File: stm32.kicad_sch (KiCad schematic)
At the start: 31 parts, among them J1 Screw_Terminal_01x04, J5 Screw_Terminal_01x08, U1 STM32H743VITx, U8 REF3030, Y1 20Mhz

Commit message: avance de pcb, se considera borneras externas para conexión de alimentación
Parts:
- removed C12: 100nF 50V, symbol Device:C
- removed C13: 1uF 50V, symbol Device:C
- removed J5: Screw_Terminal_01x08, symbol Connector:Screw_Terminal_01x08
- removed J9: ~, symbol Connector:Screw_Terminal_01x02
- added C95: 2u2F/50V, Capacitor_SMD:C_0805_2012Metric, symbol 1-Capacitor:C_0805
- added JP1: Jumper_2_Bridged, Jumper:SolderJumper-2_P1.3mm_Open_Pad1.0x1.5mm, symbol Jumper:Jumper_2_Bridged
- C74: renamed from C41; value 100nF 50V -> 100nF/50V; footprint 1-Capacitor:C_0603_1608Metric -> Capacitor_SMD:C_0603_1608Metric
- C75: renamed from C20; value ~ -> 30pF/50V; footprint (none) -> Capacitor_SMD:C_0603_1608Metric
- C76: renamed from C11; value 100nF 50V -> 100nF/50V; footprint (none) -> Capacitor_SMD:C_0603_1608Metric
- C77: renamed from C42; value 100nF 50V -> 100nF/50V; footprint 1-Capacitor:C_0603_1608Metric -> Capacitor_SMD:C_0603_1608Metric
- C78: renamed from C21; value ~ -> 30pF/50V; footprint (none) -> Capacitor_SMD:C_0603_1608Metric
- C79: renamed from C16; value 2u2F 25V -> 2u2F/50V; footprint (none) -> Capacitor_SMD:C_0805_2012Metric
- C80: renamed from C17; value 2u2F 25V -> 2u2F/50V; footprint (none) -> Capacitor_SMD:C_0805_2012Metric
- C81: renamed from C18; value 2u2F 25V -> 2u2F/50V; footprint (none) -> Capacitor_SMD:C_0805_2012Metric
- C82: renamed from C19; value 2u2F 25V -> 2u2F/50V; footprint (none) -> Capacitor_SMD:C_0805_2012Metric
- C83: renamed from C1; value 100nF 50V -> 100nF/50V; footprint (none) -> Capacitor_SMD:C_0603_1608Metric
- C84: renamed from C2; value 10nF 50V -> 10nF/50V; footprint (none) -> Capacitor_SMD:C_0603_1608Metric
- C85: renamed from C3; value 100nF 50V -> 100nF/50V; footprint (none) -> Capacitor_SMD:C_0603_1608Metric
- C86: renamed from C14; value 10nF 50V -> 10nF/50V; footprint (none) -> Capacitor_SMD:C_0603_1608Metric
- C87: renamed from C15; value 100nF 50V -> 100nF/50V; footprint (none) -> Capacitor_SMD:C_0603_1608Metric
- C88: renamed from C4; value 10nF 50V -> 10nF/50V; footprint (none) -> Capacitor_SMD:C_0603_1608Metric
- C89: renamed from C5; value 100nF 50V -> 100nF/50V; footprint (none) -> Capacitor_SMD:C_0603_1608Metric
- C90: renamed from C6; value 10nF 50V -> 10nF/50V; footprint (none) -> Capacitor_SMD:C_0603_1608Metric
- C91: renamed from C7; value 100nF 50V -> 100nF/50V; footprint (none) -> Capacitor_SMD:C_0603_1608Metric
- C92: renamed from C8; value 10nF 50V -> 10nF/50V; footprint (none) -> Capacitor_SMD:C_0603_1608Metric
- C93: renamed from C9; value 100nF 50V -> 100nF/50V; footprint (none) -> Capacitor_SMD:C_0603_1608Metric
- C94: renamed from C10; value 10nF 50V -> 10nF/50V; footprint (none) -> Capacitor_SMD:C_0603_1608Metric
- FB2: renamed from FB1; value 100R -> 600R
- J13: renamed from J1; footprint (none) -> Connector_PinHeader_2.54mm:PinHeader_1x04_P2.54mm_Vertical
- R116: renamed from R1; footprint (none) -> Resistor_SMD:R_0603_1608Metric
- Y4: renamed from Y1; value 20Mhz -> 8Mhz; footprint (none) -> Crystal:Crystal_SMD_5032-2Pin_5.0x3.2mm
- renumbered U8 to U22, U1 to U23
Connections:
- net ETH_nRST: now also JP1.1 (A); no longer U23.63 (PC6)
- net GND: now also C95.2
- net VDD_3V3: now also C95.1
- net nRST: now also JP1.2 (B)
- net Relay_8: now reaches U23.67 (PA8)
- net Relay_9: now reaches U23.68 (PA9)
- net Relay_10: now reaches U23.69 (PA10)
- net Relay_12: now reaches U23.71 (PA12)
- net CS1: now reaches U23.84 (PD3)
- net RDY2: now reaches U23.85 (PD4)
- net CS2: now reaches U23.86 (PD5)
- net DIG_1: now reaches U23.90 (PB4)
- net DIG_4: now reaches U23.93 (PB7)
- net DIG_5: now reaches U23.95 (PB8)
- net DIG_6: now reaches U23.96 (PB9)
- net DIG_7: now reaches U23.97 (PE0)
- net DIG_8: now reaches U23.98 (PE1)
- net ADC1_10: no longer names the net of U23.15 (PC0)
- net ADC1_15: no longer names the net of U23.25 (PA3)
- net ADC1_16: no longer names the net of U23.22 (PA0)
- net ADC1_18: no longer names the net of U23.28 (PA4)
- net ADC1_19: no longer names the net of U23.29 (PA5)
- net ADC1_3: no longer names the net of U23.30 (PA6)
- net ADC1_5: no longer names the net of U23.35 (PB1)
- net ADC1_9: no longer names the net of U23.34 (PB0)
- net DO1: no longer names the net of U23.55 (PD8)
- net DO2: no longer names the net of U23.56 (PD9)
- net DO3: no longer names the net of U23.57 (PD10)
- net DO4: no longer names the net of U23.58 (PD11)
- net DO5: no longer names the net of U23.59 (PD12)
- net DO6 renamed Relay_1
- net DO7 renamed Relay_2
- net DO8 renamed Relay_3
- net PLL_CLK: no longer names the net of U23.3 (PE4)
- net PLL_DIN renamed DIG_9
- net PLL_ENB: no longer names the net of U23.2 (PE3)
- net PLL_LD: no longer names the net of U23.4 (PE5)
- net PLL_RST: no longer names the net of U23.5 (PE6)
- net PWM1_1: no longer names the net of U23.39 (PE9)
- net PWM1_2: no longer names the net of U23.41 (PE11)
- net SDMMC1_CK renamed ADS_MOSI
- net SDMMC1_CMD renamed RDY1
- net SDMMC1_D0 renamed Relay_6
- net SDMMC1_D1 renamed Relay_7
- net SDMMC1_D2 renamed ADS_SCLK
- net SDMMC1_D3 renamed ADS_MISO
- net SDMMC1_SW renamed Relay_5
- net SPI2_MISO: no longer names the net of U23.17 (PC2_C)
- net SPI2_MOSI: no longer names the net of U23.18 (PC3_C)
- net SPI2_NSS renamed Relay_11
- net SPI2_SCK: no longer names the net of U23.46 (PB10)
- net UART5_RX renamed DIG_2
- net UART5_TX renamed DIG_3
- new net Relay_4: U23.63 (PC6)
- no-connect marks 31 -> 40
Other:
- note added: "C1002"
- note added: "C115962"
- note added: "C377773"
- note added: "Don't use it if it is not necessary"
- note removed: "ADC"
- note removed: "DEBUG"
- note removed: "DIGITAL OUTPUT"
- note removed: "ETHERNET"
- note removed: "HMI"
- note removed: "PWM"
- note removed: "SD CARD"
- note removed: "WIFI"
- moved on the sheet: C74, C75, C76, C77, C78, C79, C80, C81, C82, C83, C84, C85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

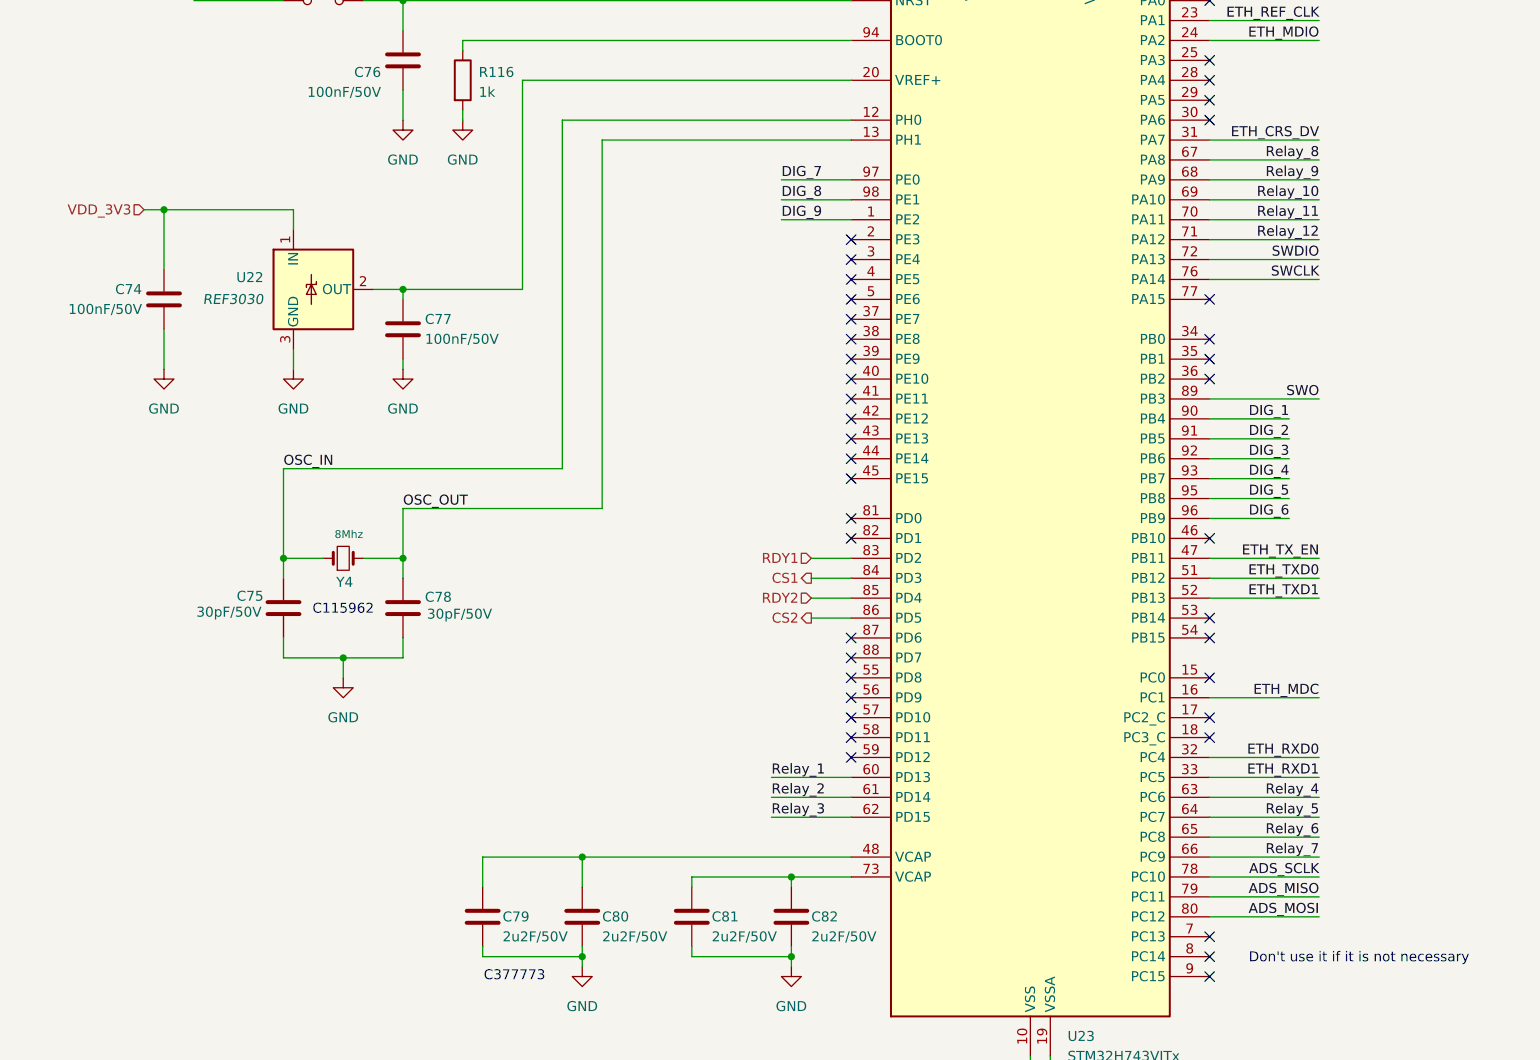
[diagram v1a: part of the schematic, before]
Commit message: Se empieza a evaluar la conexión del ethernet con la carcasa, parte analog, dig y micro en posición, tambien se busca solución para la salida de led de las entradas digitales
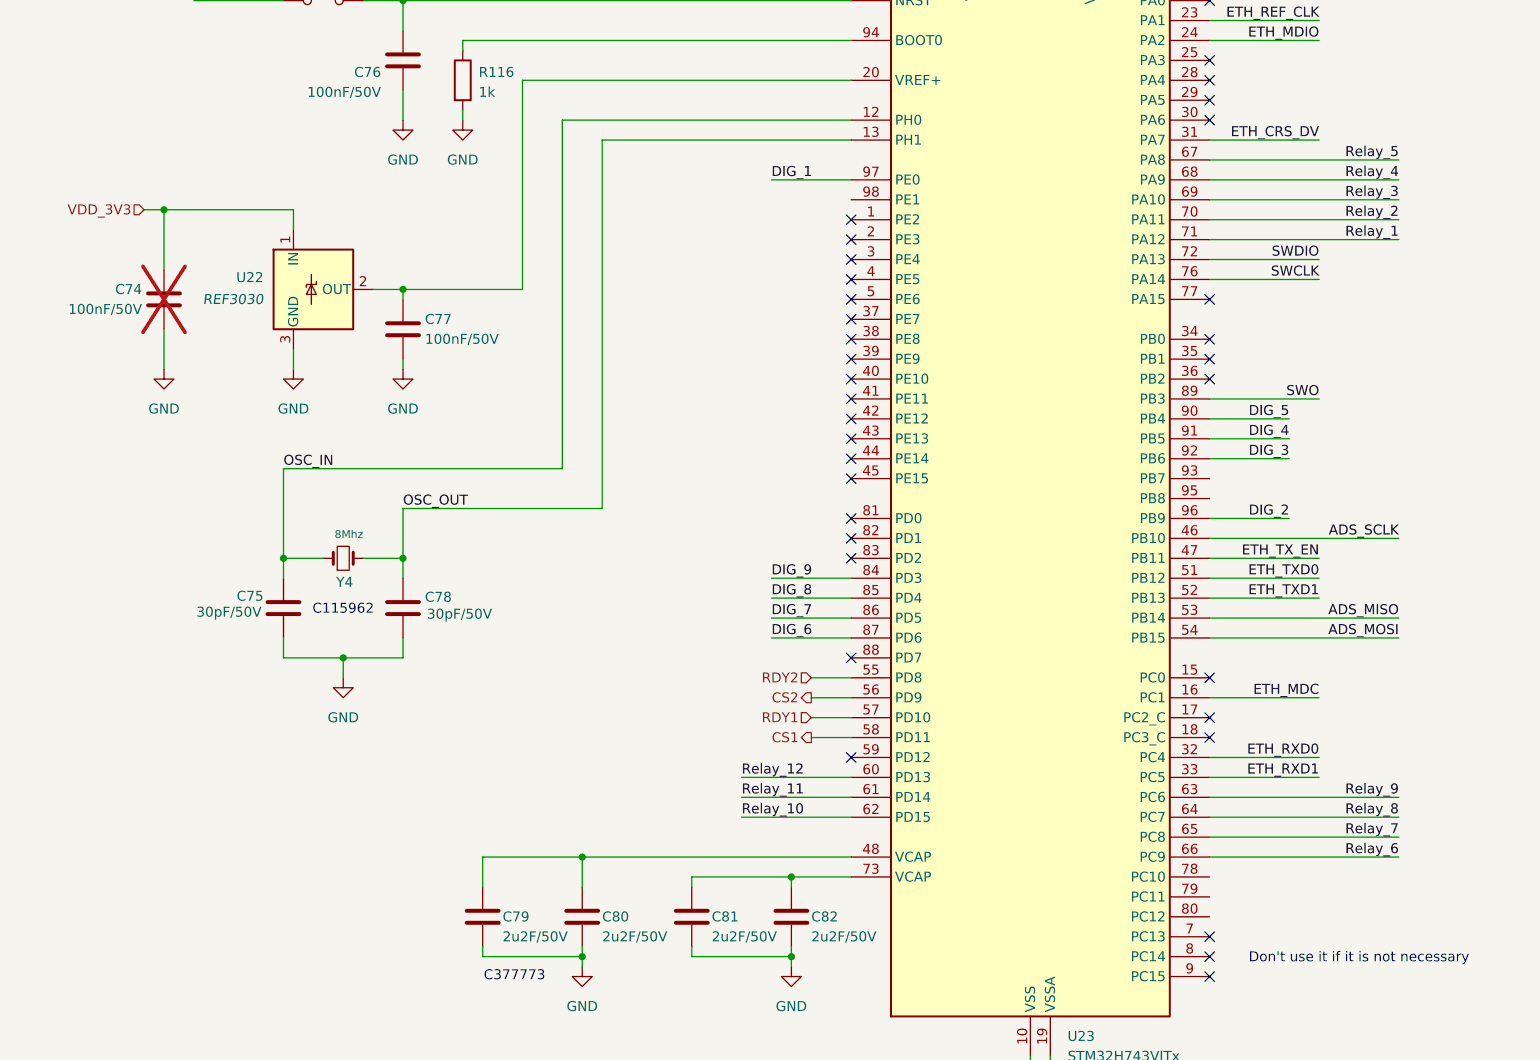
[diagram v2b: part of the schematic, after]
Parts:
- C74: now not fitted
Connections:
- net ADS_MISO: now also U23.53 (PB14); no longer U23.79 (PC11)
- net ADS_MOSI: now also U23.54 (PB15); no longer U23.80 (PC12)
- net ADS_SCLK: now also U23.46 (PB10); no longer U23.78 (PC10)
- net CS1: now also U23.58 (PD11); no longer U23.84 (PD3)
- net CS2: now also U23.56 (PD9); no longer U23.86 (PD5)
- net DIG_1: now also U23.97 (PE0); no longer U23.90 (PB4)
- net DIG_2: now also U23.96 (PB9); no longer U23.91 (PB5)
- net DIG_4: now also U23.91 (PB5); no longer U23.93 (PB7)
- net DIG_5: now also U23.90 (PB4); no longer U23.95 (PB8)
- net DIG_6: now also U23.87 (PD6); no longer U23.96 (PB9)
- net DIG_7: now also U23.86 (PD5); no longer U23.97 (PE0)
- net DIG_8: now also U23.85 (PD4); no longer U23.98 (PE1)
- net DIG_9: now also U23.84 (PD3); no longer U23.1 (PE2)
- net RDY1: now also U23.57 (PD10); no longer U23.83 (PD2)
- net RDY2: now also U23.55 (PD8); no longer U23.85 (PD4)
- net Relay_1: now also U23.71 (PA12); no longer U23.60 (PD13)
- net Relay_10: now also U23.62 (PD15); no longer U23.69 (PA10)
- net Relay_11: now also U23.61 (PD14); no longer U23.70 (PA11)
- net Relay_12: now also U23.60 (PD13); no longer U23.71 (PA12)
- net Relay_2: now also U23.70 (PA11); no longer U23.61 (PD14)
- net Relay_3: now also U23.69 (PA10); no longer U23.62 (PD15)
- net Relay_4: now also U23.68 (PA9); no longer U23.63 (PC6)
- net Relay_5: now also U23.67 (PA8); no longer U23.64 (PC7)
- net Relay_6: now also U23.66 (PC9); no longer U23.65 (PC8)
- net Relay_7: now also U23.65 (PC8); no longer U23.66 (PC9)
- net Relay_8: now also U23.64 (PC7); no longer U23.67 (PA8)
- net Relay_9: now also U23.63 (PC6); no longer U23.68 (PA9)
- no-connect marks 40 -> 34
